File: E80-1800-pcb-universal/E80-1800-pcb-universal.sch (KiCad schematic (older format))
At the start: 41 parts, among them J1 SPI, J2 OLED, J3 USB_C_Receptacle_USB2.0, Q1 AO3400A, SW1 RST, SW2 BOOT, U1 SRV05-4, U2 XC6206P332MR, U3 STM32F072RBTx

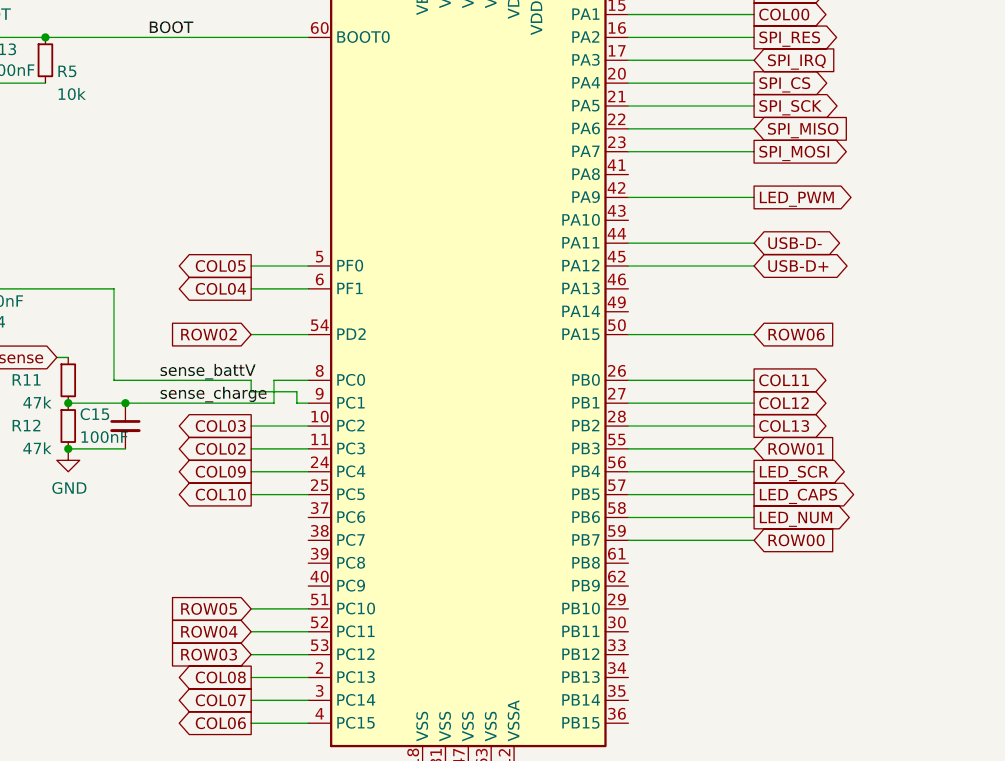
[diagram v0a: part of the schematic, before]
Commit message: wired up remaining cols
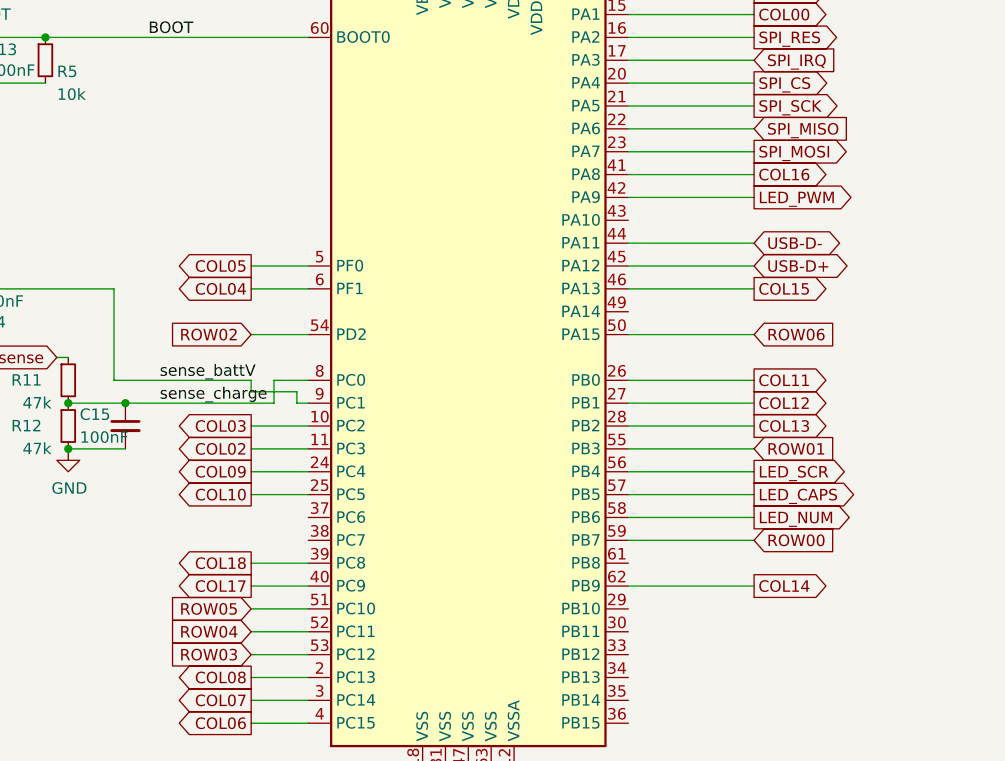
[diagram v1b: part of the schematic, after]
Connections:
- net labels added: COL14, COL15, COL16, COL17, COL18
- wire segments 167 -> 172
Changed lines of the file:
@@
 Wire Wire Line
 	4200 6350 4750 6350
+Text GLabel 4750 6750 2    50   Output ~ 0
+COL14
+Wire Wire Line
+	4750 6750 4200 6750
+Text GLabel 4750 5450 2    50   Output ~ 0
+COL15
+Wire Wire Line
+	4750 5450 4200 5450
+Text GLabel 4750 4950 2    50   Output ~ 0
+COL16
+Wire Wire Line
+	4750 4950 4200 4950
+Text GLabel 2550 6750 0    50   Output ~ 0
+COL17
+Wire Wire Line
+	2550 6750 2800 6750
+Text GLabel 2550 6650 0    50   Output ~ 0
+COL18
+Wire Wire Line
+	2550 6650 2800 6650
 $EndSCHEMATC

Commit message: continued routing
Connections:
- net labels added: I2C_SCL
- net labels removed: I2C_SCK
- wire segments 172 -> 168
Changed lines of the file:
@@
 Comment4 ""
 $EndDescr
-$Comp
-L power:GND #PWR012
-U 1 1 5E634A34
-P 900 3950
-F 0 "#PWR012" H 900 3700 50  0001 C CNN
-F 1 "GND" H 700 3900 50  0000 C CNN
-F 2 "" H 900 3950 50  0001 C CNN
-F 3 "" H 900 3950 50  0001 C CNN
-	1    900  3950
-	1    0    0    -1
-$EndComp
-$Comp
-L Device:C_Small C12
-U 1 1 5E638A0E
-P 1300 3850
-F 0 "C12" H 1392 3896 50  0000 L CNN
-F 1 "100nF" H 1392 3805 50  0000 L CNN
-F 2 "Capacitor_SMD:C_0603_1608Metric_Pad1.05x0.95mm_HandSolder" H 1300 3850 50  0001 C CNN
-F 3 "~" H 1300 3850 50  0001 C CNN
-F 4 "C1525" H 1300 3850 50  0001 C CNN "LCSC"
-	1    1300 3850
-	1    0    0    -1
-$EndComp
-Wire Wire Line
-	900  3750 900  3950
-Connection ~ 900  3950
 Text GLabel 7400 1100 2    50   Output ~ 0
 LED-
@@
 $EndComp
 Wire Wire Line
-	2700 3750 2700 4150
-Wire Wire Line
 	2700 4150 2800 4150
 Wire Wire Line
 	900  4300 900  4350
-Connection ~ 1300 3750
-Wire Wire Line
-	1300 3950 900  3950
-$Comp
-L Switch:SW_Push SW1
-U 1 1 5E6313B3
-P 1100 3750
-F 0 "SW1" H 1100 4035 50  0000 C CNN
-F 1 "RST" H 1100 3944 50  0000 C CNN
-F 2 "random-keyboard-parts:SKQG-1155865" H 1100 3950 50  0001 C CNN
-F 3 "~" H 1100 3950 50  0001 C CNN
-F 4 "C318886" H 1100 3750 50  0001 C CNN "LCSC"
-	1    1100 3750
-	1    0    0    -1
-$EndComp
 Connection ~ 1300 4350
 $Comp
@@
 	1    0    0    -1
 $EndComp
-Wire Wire Line
-	1300 3750 2700 3750
 Text Notes 7450 8000 0    50   ~ 0
 Isometria⁷⁵ - 75% blocked ISO layout keyboard
@@
 Text Label 2100 4350 0    50   ~ 0
 BOOT
-Text Label 2100 3750 0    50   ~ 0
-RST
 $Comp
 L Device:C_Small C1
@@
 	6050 1550 5400 1550
 Text GLabel 5400 1350 2    50   Input ~ 0
-I2C_SCK
+I2C_SCL
 Text GLabel 5400 1250 2    50   Input ~ 0
 I2C_SDA
@@
 	7000 4050 6500 4050
 Connection ~ 2000 5950
-Wire Wire Line
-	2650 5950 2650 5850
-Wire Wire Line
-	2650 5850 2800 5850
-Wire Wire Line
-	2000 5950 2650 5950
-Wire Wire Line
-	2550 5850 2550 5900
-Wire Wire Line
-	2550 5900 2750 5900
-Wire Wire Line
-	2750 5900 2750 5950
-Wire Wire Line
-	2750 5950 2800 5950
-Wire Wire Line
-	1950 5850 2550 5850
 Text GLabel 4750 4250 2    50   Output ~ 0
 COL00
@@
 Wire Wire Line
 	2550 6650 2800 6650
+Text GLabel 4750 6850 2    50   Output ~ 0
+I2C_SCL
+Wire Wire Line
+	4750 6850 4200 6850
+Text GLabel 4750 6950 2    50   Output ~ 0
+I2C_SDA
+Wire Wire Line
+	4750 6950 4200 6950
+Text Label 2100 3750 0    50   ~ 0
+RST
+Wire Wire Line
+	1300 3750 2700 3750
+Wire Wire Line
+	2700 3750 2700 4150
+$Comp
+L Device:C_Small C12
+U 1 1 5E638A0E
+P 1300 3850
+F 0 "C12" H 1392 3896 50  0000 L CNN
+F 1 "100nF" H 1392 3805 50  0000 L CNN
+F 2 "Capacitor_SMD:C_0603_1608Metric_Pad1.05x0.95mm_HandSolder" H 1300 3850 50  0001 C CNN
+F 3 "~" H 1300 3850 50  0001 C CNN
+F 4 "C1525" H 1300 3850 50  0001 C CNN "LCSC"
+	1    1300 3850
+	1    0    0    -1
+$EndComp
+Wire Wire Line
+	1300 3950 900  3950
+$Comp
+L power:GND #PWR012
+U 1 1 5E634A34
+P 900 3950
+F 0 "#PWR012" H 900 3700 50  0001 C CNN
+F 1 "GND" H 700 3900 50  0000 C CNN
+F 2 "" H 900 3950 50  0001 C CNN
+F 3 "" H 900 3950 50  0001 C CNN
+	1    900  3950
+	1    0    0    -1
+$EndComp
+Connection ~ 900  3950
+Wire Wire Line
+	900  3750 900  3950
+Connection ~ 1300 3750
+$Comp
+L Switch:SW_Push SW1
+U 1 1 5E6313B3
+P 1100 3750
+F 0 "SW1" H 1100 4035 50  0000 C CNN
+F 1 "RST" H 1100 3944 50  0000 C CNN
+F 2 "random-keyboard-parts:SKQG-1155865" H 1100 3950 50  0001 C CNN
+F 3 "~" H 1100 3950 50  0001 C CNN
+F 4 "C318886" H 1100 3750 50  0001 C CNN "LCSC"
+	1    1100 3750
+	1    0    0    -1
+$EndComp
+Wire Wire Line
+	1950 5850 2800 5850
+Wire Wire Line
+	2000 5950 2800 5950
 $EndSCHEMATC

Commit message: finished pcb layout, added silk labels
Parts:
- added J4: Conn_01x05, Connector_JST:JST_SH_SM05B-SRSS-TB_1x05-1MP_P1.00mm_Horizontal, symbol Connector_Generic:Conn_01x05
- added JP1: BATT, Jumper:SolderJumper-2_P1.3mm_Bridged2Bar_Pad1.0x1.5mm, symbol Device:Jumper_NC_Small
- added R1, R2: 4k7, Resistor_SMD:R_0603_1608Metric_Pad1.05x0.95mm_HandSolder, symbol Device:R_Small
- C10, C11, C3: LCSC C23733 -> C19666
- C12, C13, C14, C15, C5, C6, C7, C8, C9: LCSC C1525 -> C14663
- C2, C4: LCSC C52923 -> C15849
- F1: LCSC (none) -> C183290
- L1: LCSC (none) -> C114288
- R10: renamed from R8; LCSC C25744 -> C21190
- R11: renamed from R9; LCSC C25792 -> C25819
- R12: renamed from R10; LCSC C25792 -> C25819
- R13: renamed from R11; LCSC C25792 -> C25819
- R14: renamed from R12; LCSC C25792 -> C25819
- R3: renamed from R1; LCSC C25076 -> C22775
- R4: renamed from R2; LCSC C25744 -> C25804
- R5: renamed from R3; LCSC C25744 -> C23186
- R6: renamed from R4; LCSC C25744 -> C23186
- R7: renamed from R5; LCSC C25744 -> C25804
- R8: renamed from R6; LCSC C25744 -> C21190
- R9: renamed from R7; LCSC C25744 -> C21190
- SW1, SW2: LCSC C318886 -> (none)
- U1: LCSC (none) -> C85364
- U2: symbol Regulator_Linear:XC6206PxxxMR -> E80-1800-pcb-universal-rescue:XC6206PxxxMR-Regulator_Linear
- U3: LCSC (none) -> C46046
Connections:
- net labels added: VBUS
- wire segments 168 -> 189
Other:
- note added: "Battery connector"

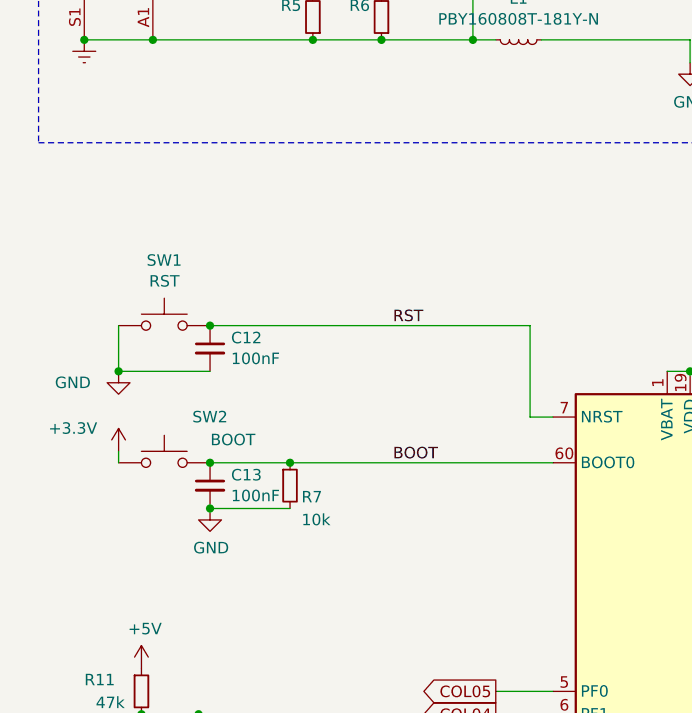
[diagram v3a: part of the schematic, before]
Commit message: improved mounting holes
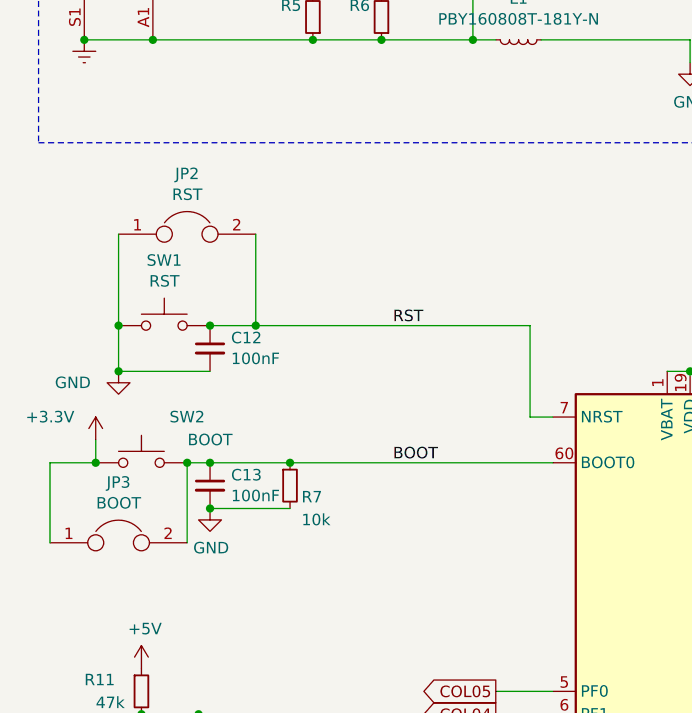
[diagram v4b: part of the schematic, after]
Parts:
- added JP2: RST, Connector_PinHeader_2.54mm:PinHeader_1x02_P2.54mm_Vertical, symbol Device:Jumper
- added JP3: BOOT, Connector_PinHeader_2.54mm:PinHeader_1x02_P2.54mm_Vertical, symbol Device:Jumper
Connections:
- net +3V3: now also JP3.1
- net BOOT: now also JP3.2
- net GND: now also JP2.1
- net RST: now also JP2.2
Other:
- moved on the sheet: SW2
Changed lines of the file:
@@
 EESchema Schematic File Version 4
-LIBS:E80-1800-pcb-universal-cache
 EELAYER 30 0
 EELAYER END
@@
 	7300 1100 7400 1100
 $Comp
-L power:GND #PWR06
+L power:GND #PWR05
 U 1 1 5E721452
 P 7300 1600
-F 0 "#PWR06" H 7300 1350 50  0001 C CNN
+F 0 "#PWR05" H 7300 1350 50  0001 C CNN
 F 1 "GND" H 7450 1600 50  0000 C CNN
 F 2 "" H 7300 1600 50  0001 C CNN
@@
 	1750 5750 1700 5750
 $Comp
-L power:GND #PWR019
+L power:GND #PWR020
 U 1 1 5E7DB3B5
 P 1750 6150
-F 0 "#PWR019" H 1750 5900 50  0001 C CNN
+F 0 "#PWR020" H 1750 5900 50  0001 C CNN
 F 1 "GND" H 1755 5977 50  0000 C CNN
 F 2 "" H 1750 6150 50  0001 C CNN
@@
 LED_PWM
 $Comp
-L power:GND #PWR04
+L power:GND #PWR03
 U 1 1 5E677479
 P 4750 1550
-F 0 "#PWR04" H 4750 1300 50  0001 C CNN
+F 0 "#PWR03" H 4750 1300 50  0001 C CNN
 F 1 "GND" H 4755 1377 50  0000 C CNN
 F 2 "" H 4750 1550 50  0001 C CNN
@@
 USB-D-
 $Comp
-L power:+5V #PWR07
+L power:+5V #PWR06
 U 1 1 5E6577C1
 P 4700 2400
-F 0 "#PWR07" H 4700 2250 50  0001 C CNN
+F 0 "#PWR06" H 4700 2250 50  0001 C CNN
 F 1 "+5V" H 4800 2500 50  0000 C CNN
 F 2 "" H 4700 2400 50  0001 C CNN
@@
 $EndComp
 $Comp
-L power:+3.3V #PWR08
+L power:+3.3V #PWR07
 U 1 1 5E625D2A
 P 5650 2400
-F 0 "#PWR08" H 5650 2250 50  0001 C CNN
+F 0 "#PWR07" H 5650 2250 50  0001 C CNN
 F 1 "+3.3V" H 5800 2500 50  0000 C CNN
 F 2 "" H 5650 2400 50  0001 C CNN
@@
 	4300 2400 4700 2400
 $Comp
-L power:GND #PWR016
+L power:GND #PWR017
 U 1 1 5E73CE85
 P 1300 4550
-F 0 "#PWR016" H 1300 4300 50  0001 C CNN
+F 0 "#PWR017" H 1300 4300 50  0001 C CNN
 F 1 "GND" H 1305 4377 50  0000 C CNN
 F 2 "" H 1300 4550 50  0001 C CNN
@@
 Connection ~ 1300 4550
 $Comp
-L power:+3.3V #PWR015
+L power:+3.3V #PWR016
 U 1 1 5E752BB1
-P 900 4300
-F 0 "#PWR015" H 900 4150 50  0001 C CNN
-F 1 "+3.3V" H 700 4400 50  0000 C CNN
-F 2 "" H 900 4300 50  0001 C CNN
-F 3 "" H 900 4300 50  0001 C CNN
-	1    900  4300
+P 800 4250
+F 0 "#PWR016" H 800 4100 50  0001 C CNN
+F 1 "+3.3V" H 600 4350 50  0000 C CNN
+F 2 "" H 800 4250 50  0001 C CNN
+F 3 "" H 800 4250 50  0001 C CNN
+	1    800  4250
 	1    0    0    -1
 $EndComp
 Wire Wire Line
 	2700 4150 2800 4150
-Wire Wire Line
-	900  4300 900  4350
-Connection ~ 1300 4350
 $Comp
 L Switch:SW_Push SW2
 U 1 1 5E73CE7F
-P 1100 4350
-F 0 "SW2" H 1300 4550 50  0000 C CNN
-F 1 "BOOT" H 1400 4450 50  0000 C CNN
-F 2 "random-keyboard-parts:SKQG-1155865" H 1100 4550 50  0001 C CNN
-F 3 "~" H 1100 4550 50  0001 C CNN
-F 4 "" H 1100 4350 50  0001 C CNN "LCSC"
-	1    1100 4350
+P 1000 4350
+F 0 "SW2" H 1200 4550 50  0000 C CNN
+F 1 "BOOT" H 1300 4450 50  0000 C CNN
+F 2 "random-keyboard-parts:SKQG-1155865" H 1000 4550 50  0001 C CNN
+F 3 "~" H 1000 4550 50  0001 C CNN
+F 4 "" H 1000 4350 50  0001 C CNN "LCSC"
+	1    1000 4350
 	1    0    0    -1
 $EndComp
@@
 Connection ~ 1000 5650
 $Comp
-L power:GND #PWR018
+L power:GND #PWR019
 U 1 1 5E8EC67C
 P 1000 5650
-F 0 "#PWR018" H 1000 5400 50  0001 C CNN
+F 0 "#PWR019" H 1000 5400 50  0001 C CNN
 F 1 "GND" H 1005 5477 50  0000 C CNN
 F 2 "" H 1000 5650 50  0001 C CNN
@@
 Connection ~ 1250 5450
 $Comp
-L power:+5V #PWR017
+L power:+5V #PWR018
 U 1 1 5E93AEEB
 P 1000 5250
-F 0 "#PWR017" H 1000 5100 50  0001 C CNN
+F 0 "#PWR018" H 1000 5100 50  0001 C CNN
 F 1 "+5V" H 1015 5423 50  0000 C CNN
 F 2 "" H 1000 5250 50  0001 C CNN
@@
 $EndComp
 $Comp
-L power:GND #PWR011
+L power:GND #PWR012
 U 1 1 5E626CC8
 P 5250 2700
-F 0 "#PWR011" H 5250 2450 50  0001 C CNN
+F 0 "#PWR012" H 5250 2450 50  0001 C CNN
 F 1 "GND" H 5255 2527 50  0000 C CNN
 F 2 "" H 5250 2700 50  0001 C CNN
@@
 	3600 7550 3700 7550
 $Comp
-L power:GND #PWR020
+L power:GND #PWR021
 U 1 1 5F4FB013
 P 3300 7550
-F 0 "#PWR020" H 3300 7300 50  0001 C CNN
+F 0 "#PWR021" H 3300 7300 50  0001 C CNN
 F 1 "GND" H 3305 7377 50  0000 C CNN
 F 2 "" H 3300 7550 50  0001 C CNN
@@
 Connection ~ 3300 7550
 $Comp
-L power:+3.3V #PWR013
+L power:+3.3V #PWR014
 U 1 1 5F4FBD06
 P 3800 3950
-F 0 "#PWR013" H 3800 3800 50  0001 C CNN
+F 0 "#PWR014" H 3800 3800 50  0001 C CNN
 F 1 "+3.3V" H 3950 4050 50  0000 C CNN
 F 2 "" H 3800 3950 50  0001 C CNN
@@
 $EndComp
 $Comp
-L power:GND #PWR05
+L power:GND #PWR04
 U 1 1 5F53F5D8
 P 6050 1550
-F 0 "#PWR05" H 6050 1300 50  0001 C CNN
+F 0 "#PWR04" H 6050 1300 50  0001 C CNN
 F 1 "GND" H 6055 1377 50  0000 C CNN
 F 2 "" H 6050 1550 50  0001 C CNN
@@
 $EndComp
 $Comp
-L power:+3.3V #PWR02
+L power:+3.3V #PWR01
 U 1 1 5E83E1D4
 P 4750 850
-F 0 "#PWR02" H 4750 700 50  0001 C CNN
+F 0 "#PWR01" H 4750 700 50  0001 C CNN
 F 1 "+3.3V" H 4600 950 50  0000 C CNN
 F 2 "" H 4750 850 50  0001 C CNN
@@
 $EndComp
 $Comp
-L power:+3.3V #PWR03
+L power:+3.3V #PWR02
 U 1 1 5F54229D
 P 6050 850
-F 0 "#PWR03" H 6050 700 50  0001 C CNN
+F 0 "#PWR02" H 6050 700 50  0001 C CNN
 F 1 "+3.3V" H 5900 950 50  0000 C CNN
 F 2 "" H 6050 850 50  0001 C CNN
@@
 	1900 1200 3000 1200
 $Comp
-L power:Earth #PWR09
+L power:Earth #PWR08
 U 1 1 5F049598
 P 750 2500
-F 0 "#PWR09" H 750 2250 50  0001 C CNN
+F 0 "#PWR08" H 750 2250 50  0001 C CNN
 F 1 "Earth" H 750 2350 50  0001 C CNN
 F 2 "" H 750 2500 50  0001 C CNN
@@
 	7500 4600 7500 4700
 $Comp
-L power:+3.3V #PWR014
+L power:+3.3V #PWR015
 U 1 1 5F1AFDAE
 P 7000 3950
-F 0 "#PWR014" H 7000 3800 50  0001 C CNN
+F 0 "#PWR015" H 7000 3800 50  0001 C CNN
 F 1 "+3.3V" H 7150 4050 50  0000 C CNN
 F 2 "" H 7000 3950 50  0001 C CNN
@@
 RST
 Wire Wire Line
-	1300 3750 2700 3750
+	1300 3750 1500 3750
 Wire Wire Line
 	2700 3750 2700 4150
@@
 	1300 3950 900  3950
 $Comp
-L power:GND #PWR012
+L power:GND #PWR013
 U 1 1 5E634A34
 P 900 3950
-F 0 "#PWR012" H 900 3700 50  0001 C CNN
+F 0 "#PWR013" H 900 3700 50  0001 C CNN
 F 1 "GND" H 700 3900 50  0000 C CNN
 F 2 "" H 900 3950 50  0001 C CNN
@@
 	10150 2400 9950 2400
 $Comp
-L power:+5V #PWR01
+L power:+5V #PWR09
 U 1 1 5F0BBFC0
 P 10650 2500
-F 0 "#PWR01" H 10650 2350 50  0001 C CNN
+F 0 "#PWR09" H 10650 2350 50  0001 C CNN
 F 1 "+5V" H 10750 2500 50  0000 C CNN
 F 2 "" H 10650 2500 50  0001 C CNN
@@
 	9950 2800 10450 2800
 $Comp
-L power:GND #PWR021
+L power:GND #PWR011
 U 1 1 5F114368
 P 10650 2600
-F 0 "#PWR021" H 10650 2350 50  0001 C CNN
+F 0 "#PWR011" H 10650 2350 50  0001 C CNN
 F 1 "GND" H 10750 2600 50  0000 C CNN
 F 2 "" H 10650 2600 50  0001 C CNN
@@
 Text Notes 9550 2050 0    50   ~ 0
 Battery connector
+$Comp
+L Device:Jumper JP2
+U 1 1 5F5EA723
+P 1200 3350
+F 0 "JP2" H 1200 3614 50  0000 C CNN
+F 1 "RST" H 1200 3523 50  0000 C CNN
+F 2 "Connector_PinHeader_2.54mm:PinHeader_1x02_P2.54mm_Vertical" H 1200 3350 50  0001 C CNN
+F 3 "~" H 1200 3350 50  0001 C CNN
+	1    1200 3350
+	1    0    0    -1
+$EndComp
+Wire Wire Line
+	900  3350 900  3750
+Connection ~ 900  3750
+Wire Wire Line
+	1500 3350 1500 3750
+Connection ~ 1500 3750
+Wire Wire Line
+	1500 3750 2700 3750
+$Comp
+L Device:Jumper JP3
+U 1 1 5F602145
+P 900 4700
+F 0 "JP3" H 900 4964 50  0000 C CNN
+F 1 "BOOT" H 900 4873 50  0000 C CNN
+F 2 "Connector_PinHeader_2.54mm:PinHeader_1x02_P2.54mm_Vertical" H 900 4700 50  0001 C CNN
+F 3 "~" H 900 4700 50  0001 C CNN
+	1    900  4700
+	1    0    0    -1
+$EndComp
+Wire Wire Line
+	1200 4350 1300 4350
+Connection ~ 1300 4350
+Wire Wire Line
+	1200 4700 1200 4350
+Connection ~ 1200 4350
+Wire Wire Line
+	600  4700 600  4350
+Wire Wire Line
+	600  4350 800  4350
+Wire Wire Line
+	800  4350 800  4250
+Connection ~ 800  4350
 $EndSCHEMATC

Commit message: minor routing changes
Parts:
- added C1: 10uF, kicad-keyboard-parts:CP_EIA-3216-18_Kemet-A_stealth, symbol Device:C_Small
- C10: renamed from C9; footprint Capacitor_SMD:C_0603_1608Metric_Pad1.05x0.95mm_HandSolder -> kicad-keyboard-parts:C_0603_1608Metric_stealth
- C11: renamed from C10; footprint Capacitor_SMD:C_0603_1608Metric_Pad1.05x0.95mm_HandSolder -> kicad-keyboard-parts:C_0603_1608Metric_stealth
- C12: renamed from C11; footprint Capacitor_SMD:C_0603_1608Metric_Pad1.05x0.95mm_HandSolder -> kicad-keyboard-parts:C_0603_1608Metric_stealth
- C13: renamed from C12; footprint Capacitor_SMD:C_0603_1608Metric_Pad1.05x0.95mm_HandSolder -> kicad-keyboard-parts:C_0603_1608Metric_stealth
- C14: renamed from C13; footprint Capacitor_SMD:C_0603_1608Metric_Pad1.05x0.95mm_HandSolder -> kicad-keyboard-parts:C_0603_1608Metric_stealth
- C15: renamed from C14; footprint Capacitor_SMD:C_0603_1608Metric_Pad1.05x0.95mm_HandSolder -> kicad-keyboard-parts:C_0603_1608Metric_stealth
- C16: renamed from C15; footprint Capacitor_SMD:C_0603_1608Metric_Pad1.05x0.95mm_HandSolder -> kicad-keyboard-parts:C_0603_1608Metric_stealth
- C2: renamed from C1; footprint Capacitor_Tantalum_SMD:CP_EIA-3216-18_Kemet-A -> kicad-keyboard-parts:CP_EIA-3216-18_Kemet-A_stealth
- C3: renamed from C2; footprint Capacitor_SMD:C_0603_1608Metric_Pad1.05x0.95mm_HandSolder -> kicad-keyboard-parts:C_0603_1608Metric_stealth
- C4: renamed from C3; footprint Capacitor_SMD:C_0603_1608Metric_Pad1.05x0.95mm_HandSolder -> kicad-keyboard-parts:C_0603_1608Metric_stealth
- C5: renamed from C4; footprint Capacitor_SMD:C_0603_1608Metric_Pad1.05x0.95mm_HandSolder -> kicad-keyboard-parts:C_0603_1608Metric_stealth
- C6: renamed from C5; footprint Capacitor_SMD:C_0603_1608Metric_Pad1.05x0.95mm_HandSolder -> kicad-keyboard-parts:C_0603_1608Metric_stealth
- C7: renamed from C6; footprint Capacitor_SMD:C_0603_1608Metric_Pad1.05x0.95mm_HandSolder -> kicad-keyboard-parts:C_0603_1608Metric_stealth
- C8: renamed from C7; footprint Capacitor_SMD:C_0603_1608Metric_Pad1.05x0.95mm_HandSolder -> kicad-keyboard-parts:C_0603_1608Metric_stealth
- C9: renamed from C8; footprint Capacitor_SMD:C_0603_1608Metric_Pad1.05x0.95mm_HandSolder -> kicad-keyboard-parts:C_0603_1608Metric_stealth
- J4: value Conn_01x05 -> BATT
- Q1: footprint Package_TO_SOT_SMD:SOT-23 -> kicad-keyboard-parts:SOT-23_stealth
- R1, R10, R11, R12, R13, R14, R2, R3, R4, R5, R6, R7, R8, R9: footprint Resistor_SMD:R_0603_1608Metric_Pad1.05x0.95mm_HandSolder -> kicad-keyboard-parts:R_0603_1608Metric_stealth
- SW1, SW2: footprint random-keyboard-parts:SKQG-1155865 -> Button_Switch_SMD:SW_SPST_SKQG_WithoutStem
- U2: footprint Package_TO_SOT_SMD:SOT-23 -> kicad-keyboard-parts:SOT-23_stealth; symbol E80-1800-pcb-universal-rescue:XC6206PxxxMR-Regulator_Linear -> kicad-keyboard-parts:XC6206PxxxMR-Regulator_Linear
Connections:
- net +5V: now also C1.1
- net GND: now also C1.2
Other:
- moved on the sheet: C10, C11, C12, C2, C3, C4, C5, C6, C7, C8, C9, U2
